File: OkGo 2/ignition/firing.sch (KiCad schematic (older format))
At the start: 43 parts

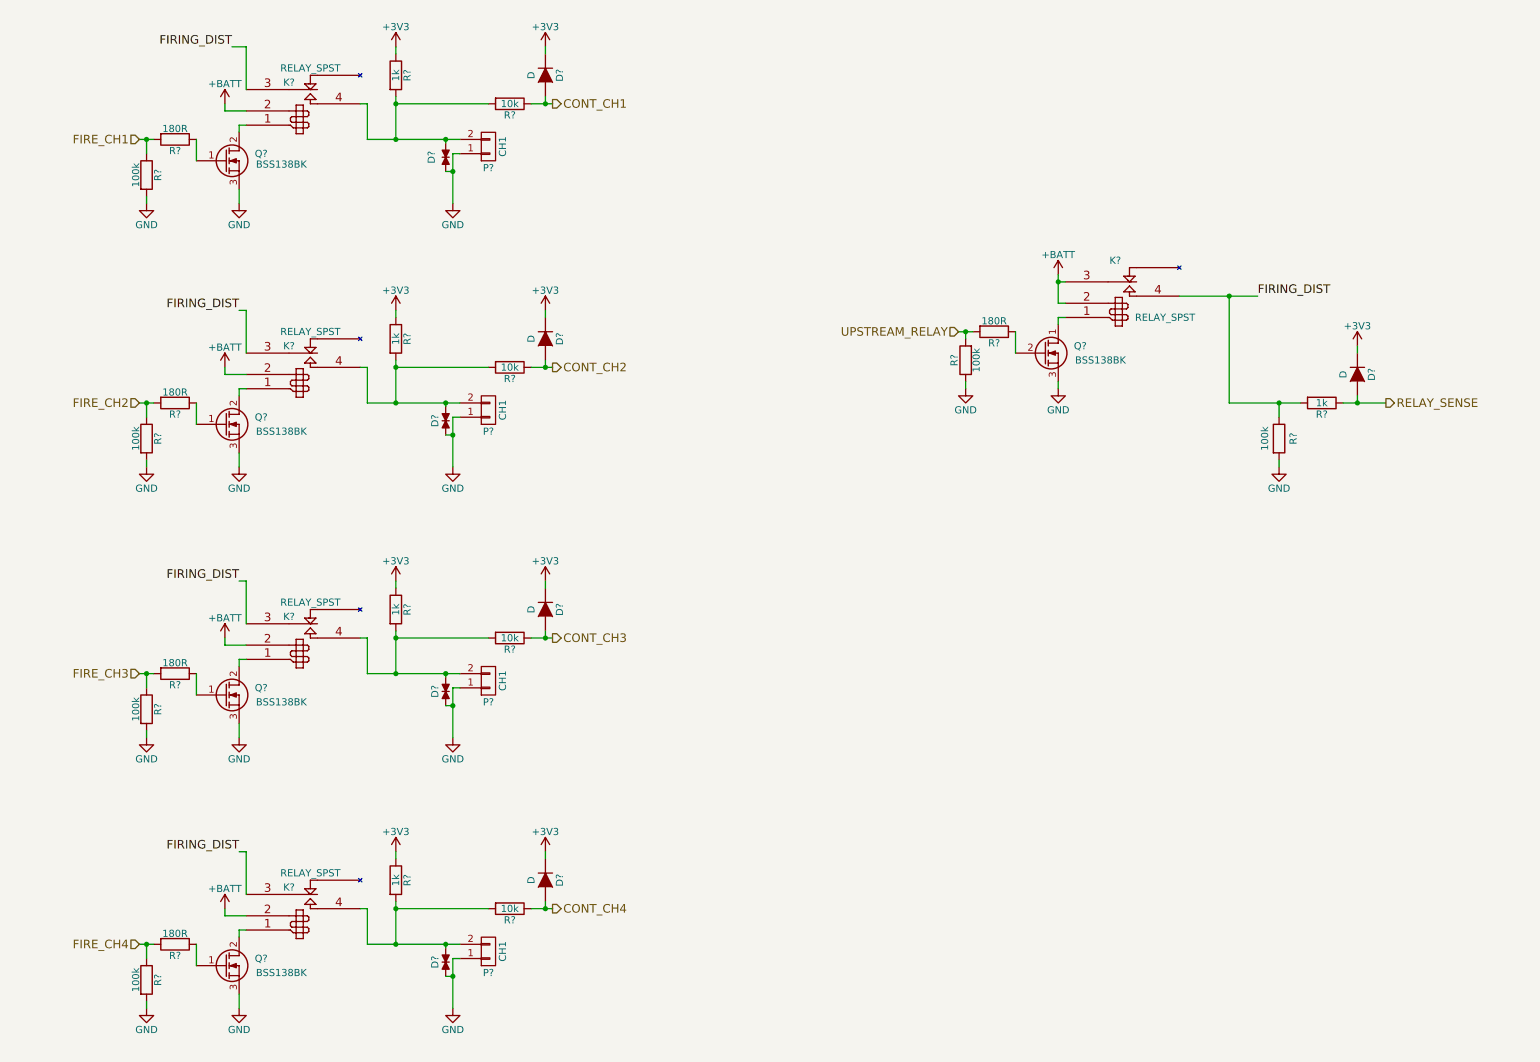
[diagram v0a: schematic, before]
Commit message: Test points. Resolves #14
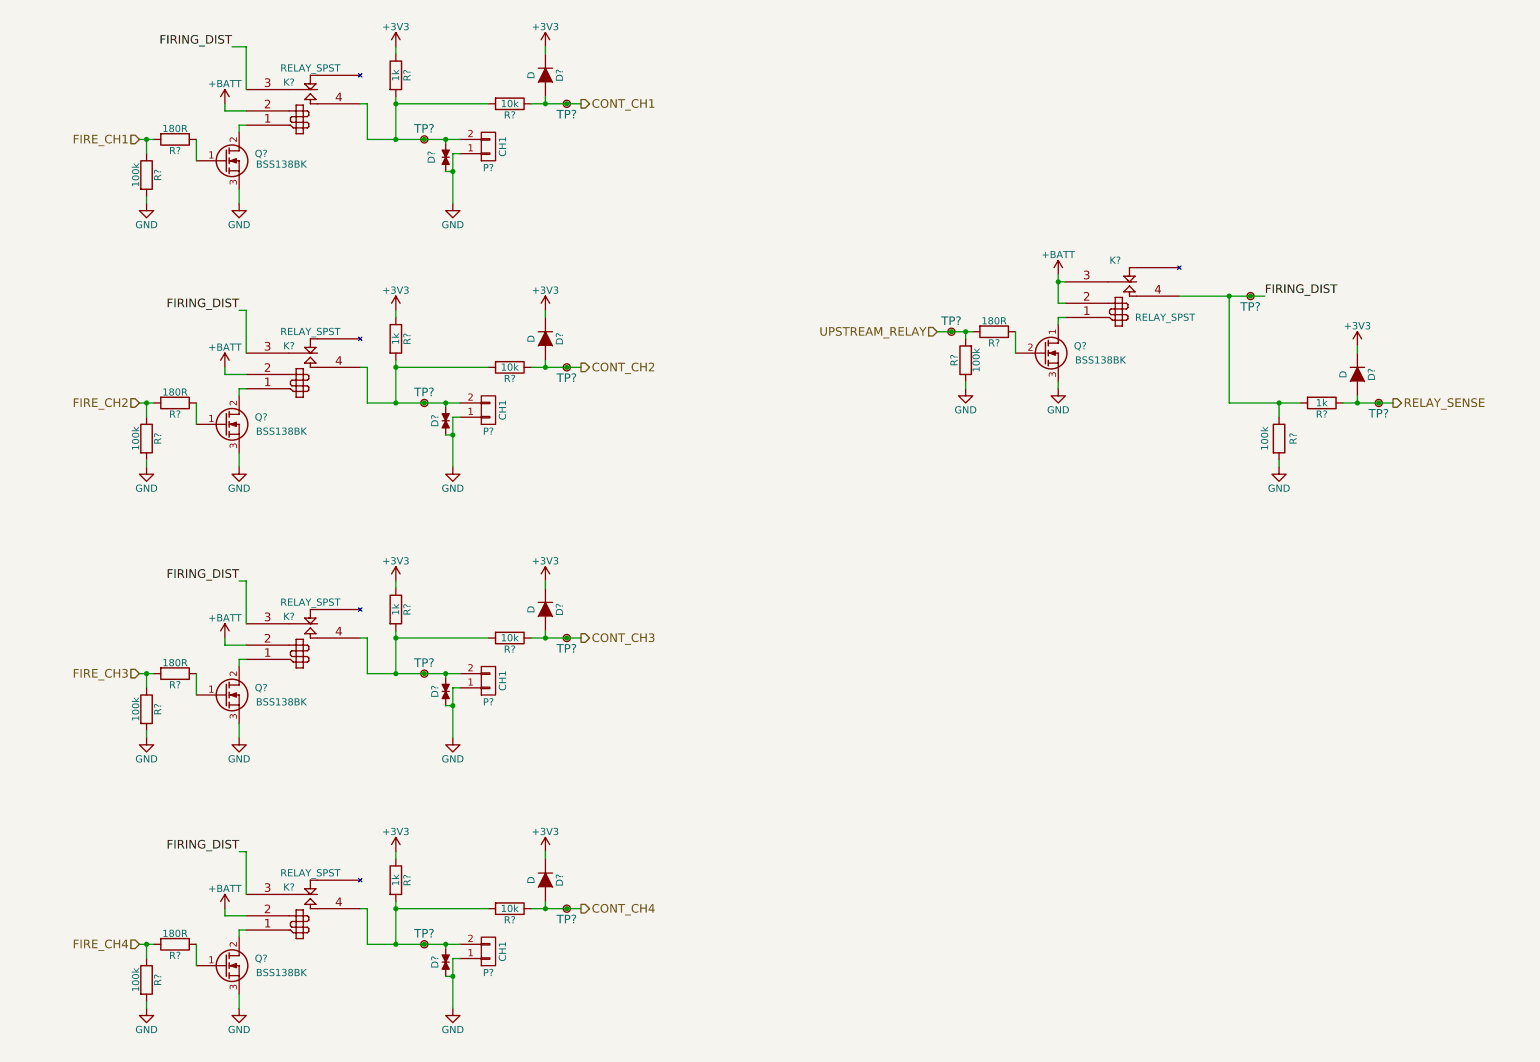
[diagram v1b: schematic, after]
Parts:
- added TP? (x11): TestPoint, symbol TestPoint
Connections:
- net CONT_CH1: now also TP?.1
- net CONT_CH2: now also TP?.1
- net CONT_CH3: now also TP?.1
- net CONT_CH4: now also TP?.1
- net FIRING_DIST: now also TP?.1
- net RELAY_SENSE: now also TP?.1
- net UPSTREAM_RELAY: now also TP?.1
- net at D?.1, K?.4, P?.2 (P2)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: now also TP?.1
- net at D?.2, K?.4, P?.2 (P2)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: now also TP?.1 (x3)
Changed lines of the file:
@@
 LIBS:stm32f071cbt6
 LIBS:tvs_small
+LIBS:testpoint
 LIBS:ignition-cache
 EELAYER 25 0
@@
 	7850 3150 7850 3100
 Wire Wire Line
-	7150 2750 7200 2750
+	7000 2750 7100 2750
+Wire Wire Line
+	7100 2750 7200 2750
 Wire Wire Line
 	7200 2750 7250 2750
@@
 	8700 2500 9050 2500
 Wire Wire Line
-	9050 2500 9250 2500
+	9050 2500 9200 2500
+Wire Wire Line
+	9200 2500 9300 2500
 Wire Wire Line
 	9050 2500 9050 3250
@@
 	9850 3250 9950 3250
 Wire Wire Line
-	9950 3250 10150 3250
+	9950 3250 10100 3250
+Wire Wire Line
+	10100 3250 10200 3250
 $Comp
 L CONN_01X02 P?
@@
 	4150 1150 4250 1150
 Wire Wire Line
-	4250 1150 4300 1150
+	4250 1150 4400 1150
+Wire Wire Line
+	4400 1150 4500 1150
 Wire Wire Line
 	3200 1100 3200 1150
@@
 	4150 3000 4250 3000
 Wire Wire Line
-	4250 3000 4300 3000
+	4250 3000 4400 3000
+Wire Wire Line
+	4400 3000 4500 3000
 Wire Wire Line
 	3200 2950 3200 3000
@@
 	4150 4900 4250 4900
 Wire Wire Line
-	4250 4900 4300 4900
+	4250 4900 4400 4900
+Wire Wire Line
+	4400 4900 4500 4900
 Wire Wire Line
 	3200 4850 3200 4900
@@
 	4150 6800 4250 6800
 Wire Wire Line
-	4250 6800 4300 6800
+	4250 6800 4400 6800
+Wire Wire Line
+	4400 6800 4500 6800
 Wire Wire Line
 	3200 6750 3200 6800
@@
 Wire Wire Line
 	2000 1200 2150 1200
-Text HLabel 4300 1150 2    60   Output ~ 0
+Text HLabel 4500 1150 2    60   Output ~ 0
 CONT_CH1
-Text HLabel 4300 3000 2    60   Output ~ 0
+Text HLabel 4500 3000 2    60   Output ~ 0
 CONT_CH2
-Text HLabel 4300 4900 2    60   Output ~ 0
+Text HLabel 4500 4900 2    60   Output ~ 0
 CONT_CH3
-Text HLabel 4300 6800 2    60   Output ~ 0
+Text HLabel 4500 6800 2    60   Output ~ 0
 CONT_CH4
 Text HLabel 1400 7050 0    60   Input ~ 0
@@
 Text HLabel 1400 1400 0    60   Input ~ 0
 FIRE_CH1
-Text HLabel 7150 2750 0    60   Input ~ 0
+Text HLabel 7000 2750 0    60   Input ~ 0
 UPSTREAM_RELAY
-Text HLabel 10150 3250 2    60   Output ~ 0
+Text HLabel 10200 3250 2    60   Output ~ 0
 RELAY_SENSE
 Text Label 2050 750  2    60   ~ 0
@@
 Text Label 2100 6400 2    60   ~ 0
 FIRING_DIST
-Text Label 9250 2500 0    60   ~ 0
+Text Label 9300 2500 0    60   ~ 0
 FIRING_DIST
+$Comp
+L TestPoint TP?
+U 1 1 559DCEAD
+P 4400 1150
+F 0 "TP?" H 4400 1075 60  0000 C CNN
+F 1 "TestPoint" H 4375 975 60  0001 C CNN
+F 2 "" H 4400 1150 60  0000 C CNN
+F 3 "" H 4400 1150 60  0000 C CNN
+	1    4400 1150
+	1    0    0    -1
+$EndComp
+Connection ~ 4400 1150
+$Comp
+L TestPoint TP?
+U 1 1 559DD237
+P 4400 3000
+F 0 "TP?" H 4400 2925 60  0000 C CNN
+F 1 "TestPoint" H 4375 2825 60  0001 C CNN
+F 2 "" H 4400 3000 60  0000 C CNN
+F 3 "" H 4400 3000 60  0000 C CNN
+	1    4400 3000
+	1    0    0    -1
+$EndComp
+Connection ~ 4400 3000
+$Comp
+L TestPoint TP?
+U 1 1 559DD3E6
+P 4400 4900
+F 0 "TP?" H 4400 4825 60  0000 C CNN
+F 1 "TestPoint" H 4375 4725 60  0001 C CNN
+F 2 "" H 4400 4900 60  0000 C CNN
+F 3 "" H 4400 4900 60  0000 C CNN
+	1    4400 4900
+	1    0    0    -1
+$EndComp
+Connection ~ 4400 4900
+$Comp
+L TestPoint TP?
+U 1 1 559DD5CC
+P 4400 6800
+F 0 "TP?" H 4400 6725 60  0000 C CNN
+F 1 "TestPoint" H 4375 6625 60  0001 C CNN
+F 2 "" H 4400 6800 60  0000 C CNN
+F 3 "" H 4400 6800 60  0000 C CNN
+	1    4400 6800
+	1    0    0    -1
+$EndComp
+Connection ~ 4400 6800
+$Comp
+L TestPoint TP?
+U 1 1 559DDAEE
+P 7100 2750
+F 0 "TP?" H 7100 2675 60  0000 C CNN
+F 1 "TestPoint" H 7075 2575 60  0001 C CNN
+F 2 "" H 7100 2750 60  0000 C CNN
+F 3 "" H 7100 2750 60  0000 C CNN
+	1    7100 2750
+	-1   0    0    1
+$EndComp
+Connection ~ 7100 2750
+$Comp
+L TestPoint TP?
+U 1 1 559DDDE6
+P 10100 3250
+F 0 "TP?" H 10100 3175 60  0000 C CNN
+F 1 "TestPoint" H 10075 3075 60  0001 C CNN
+F 2 "" H 10100 3250 60  0000 C CNN
+F 3 "" H 10100 3250 60  0000 C CNN
+	1    10100 3250
+	1    0    0    -1
+$EndComp
+Connection ~ 10100 3250
+$Comp
+L TestPoint TP?
+U 1 1 559DE049
+P 9200 2500
+F 0 "TP?" H 9200 2425 60  0000 C CNN
+F 1 "TestPoint" H 9175 2325 60  0001 C CNN
+F 2 "" H 9200 2500 60  0000 C CNN
+F 3 "" H 9200 2500 60  0000 C CNN
+	1    9200 2500
+	1    0    0    -1
+$EndComp
+Connection ~ 9200 2500
+$Comp
+L TestPoint TP?
+U 1 1 559DE905
+P 3400 1400
+F 0 "TP?" H 3400 1325 60  0000 C CNN
+F 1 "TestPoint" H 3375 1225 60  0001 C CNN
+F 2 "" H 3400 1400 60  0000 C CNN
+F 3 "" H 3400 1400 60  0000 C CNN
+	1    3400 1400
+	-1   0    0    1
+$EndComp
+Connection ~ 3400 1400
+$Comp
+L TestPoint TP?
+U 1 1 559DF1B5
+P 3400 3250
+F 0 "TP?" H 3400 3175 60  0000 C CNN
+F 1 "TestPoint" H 3375 3075 60  0001 C CNN
+F 2 "" H 3400 3250 60  0000 C CNN
+F 3 "" H 3400 3250 60  0000 C CNN
+	1    3400 3250
+	-1   0    0    1
+$EndComp
+Connection ~ 3400 3250
+$Comp
+L TestPoint TP?
+U 1 1 559DF3AE
+P 3400 5150
+F 0 "TP?" H 3400 5075 60  0000 C CNN
+F 1 "TestPoint" H 3375 4975 60  0001 C CNN
+F 2 "" H 3400 5150 60  0000 C CNN
+F 3 "" H 3400 5150 60  0000 C CNN
+	1    3400 5150
+	-1   0    0    1
+$EndComp
+Connection ~ 3400 5150
+$Comp
+L TestPoint TP?
+U 1 1 559DF5E5
+P 3400 7050
+F 0 "TP?" H 3400 6975 60  0000 C CNN
+F 1 "TestPoint" H 3375 6875 60  0001 C CNN
+F 2 "" H 3400 7050 60  0000 C CNN
+F 3 "" H 3400 7050 60  0000 C CNN
+	1    3400 7050
+	-1   0    0    1
+$EndComp
+Connection ~ 3400 7050
 $EndSCHEMATC

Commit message: Specced/valued/footprinted a lot of parts
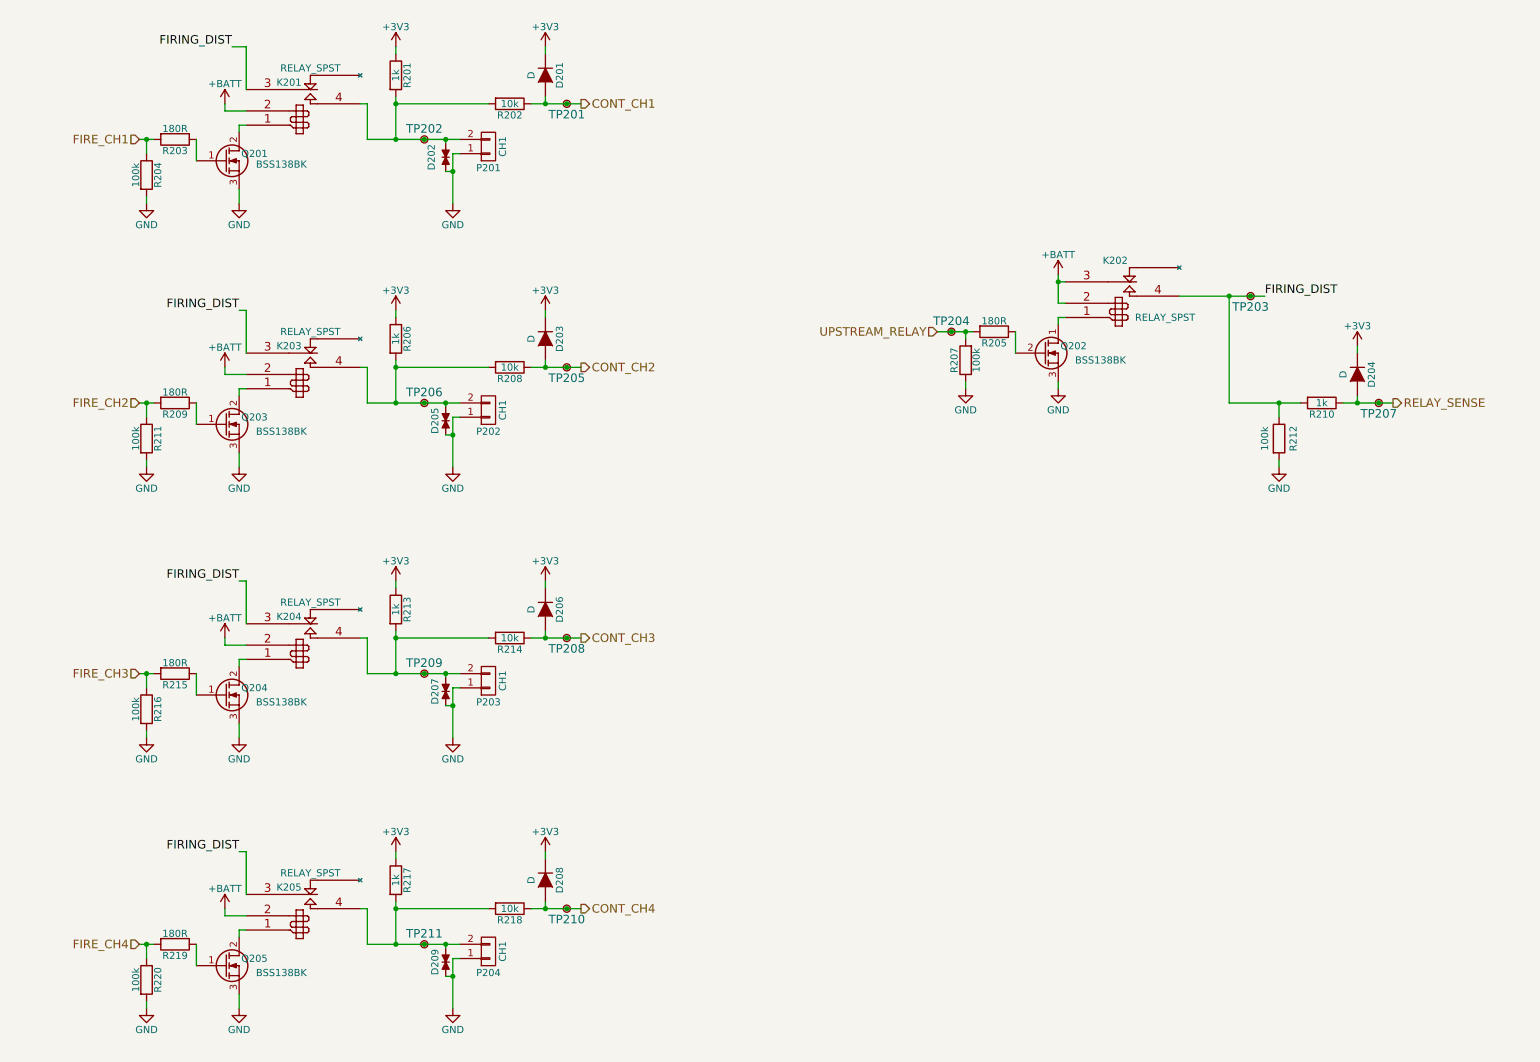
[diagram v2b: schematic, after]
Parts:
- D201, D203, D204, D206, D208: renamed from D?; footprint (none) -> Diodes_SMD:SOD-123; Farnell (none) -> 1510671
- K201, K203, K204, K205: renamed from K?; Farnell 1891999 -> 1629044
- K202: renamed from K?; Farnell (none) -> 1629044
- R201, R206, R210, R213, R217: renamed from R?; footprint (none) -> Resistors_SMD:R_0805_HandSoldering; Farnell (none) -> 2331796
- R202, R208, R214, R218: renamed from R?; footprint (none) -> Resistors_SMD:R_0805_HandSoldering; Farnell (none) -> 2331808
- R203, R205, R209, R215, R219: renamed from R?; footprint (none) -> Resistors_SMD:R_0805_HandSoldering; Farnell (none) -> 2331786
- R204, R207, R211, R212, R216, R220: renamed from R?; footprint (none) -> Resistors_SMD:R_0805_HandSoldering; Farnell (none) -> 2331783
- gave numbers to parts that had none: 24

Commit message: Lots and lots of part selections and small mods
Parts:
- added D?: RED, symbol LED_R
- added D?: GREEN, symbol LED_R
- added D?: BLUE, symbol LED_R
- added D?: WHITE, symbol LED_R
- added P?: CH1, symbol CONN_01X02
- added P?: CH2, symbol CONN_01X02
- added P?: CH3, symbol CONN_01X02
- added P?: CH4, symbol CONN_01X02
- P202: value CH1 -> CH2
- P203: value CH1 -> CH3
- P204: value CH1 -> CH4
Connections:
- new net: D?.1 (K), P?.1 (P1) (x4)
- new net: D?.2 (A), P?.2 (P2) (x4)
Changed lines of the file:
@@
 LIBS:tvs_small
 LIBS:testpoint
+LIBS:sma
+LIBS:led_r
+LIBS:lipo_3s
+LIBS:spst_small
 LIBS:ignition-cache
 EELAYER 25 0
@@
 U 1 1 559E5DC4
 P 3850 1450
-F 0 "P201" H 3850 1600 50  0000 C CNN
-F 1 "CH1" V 3950 1450 50  0000 C CNN
+F 0 "P201" H 3800 1300 50  0000 C CNN
+F 1 "CH1" H 3850 1600 50  0000 C CNN
 F 2 "" H 3850 1450 60  0000 C CNN
 F 3 "" H 3850 1450 60  0000 C CNN
@@
 U 1 1 559E5E1D
 P 3850 3300
-F 0 "P202" H 3850 3450 50  0000 C CNN
-F 1 "CH1" V 3950 3300 50  0000 C CNN
+F 0 "P202" H 3800 3150 50  0000 C CNN
+F 1 "CH2" H 3850 3450 50  0000 C CNN
 F 2 "" H 3850 3300 60  0000 C CNN
 F 3 "" H 3850 3300 60  0000 C CNN
@@
 U 1 1 559E5E76
 P 3850 5200
-F 0 "P203" H 3850 5350 50  0000 C CNN
-F 1 "CH1" V 3950 5200 50  0000 C CNN
+F 0 "P203" H 3800 5050 50  0000 C CNN
+F 1 "CH3" H 3850 5350 50  0000 C CNN
 F 2 "" H 3850 5200 60  0000 C CNN
 F 3 "" H 3850 5200 60  0000 C CNN
@@
 U 1 1 559E5ECF
 P 3850 7100
-F 0 "P204" H 3850 7250 50  0000 C CNN
-F 1 "CH1" V 3950 7100 50  0000 C CNN
+F 0 "P204" H 3800 6950 50  0000 C CNN
+F 1 "CH4" H 3850 7250 50  0000 C CNN
 F 2 "" H 3850 7100 60  0000 C CNN
 F 3 "" H 3850 7100 60  0000 C CNN
@@
 $EndComp
 Connection ~ 3400 7050
+$Comp
+L LED_R D?
+U 1 1 559F6774
+P 4300 1600
+F 0 "D?" H 4275 1725 60  0000 C CNN
+F 1 "RED" H 4250 1800 60  0000 C CNN
+F 2 "" H 4400 1800 60  0000 C CNN
+F 3 "" H 4400 1800 60  0000 C CNN
+F 4 "SC09351" H 4300 1600 60  0001 C CNN "Farnell"
+	1    4300 1600
+	0    1    1    0
+$EndComp
+$Comp
+L CONN_01X02 P?
+U 1 1 559F700F
+P 4000 1450
+F 0 "P?" H 4000 1300 50  0000 C CNN
+F 1 "CH1" H 4000 1600 50  0000 C CNN
+F 2 "" H 4000 1450 60  0000 C CNN
+F 3 "" H 4000 1450 60  0000 C CNN
+	1    4000 1450
+	-1   0    0    1
+$EndComp
+Wire Wire Line
+	4200 1400 4300 1400
+Wire Wire Line
+	4200 1500 4200 1800
+Wire Wire Line
+	4200 1800 4300 1800
+$Comp
+L LED_R D?
+U 1 1 559F7DE2
+P 4300 3450
+F 0 "D?" H 4275 3575 60  0000 C CNN
+F 1 "GREEN" H 4250 3650 60  0000 C CNN
+F 2 "" H 4400 3650 60  0000 C CNN
+F 3 "" H 4400 3650 60  0000 C CNN
+F 4 "SC09352" H 4300 3450 60  0001 C CNN "Farnell"
+	1    4300 3450
+	0    1    1    0
+$EndComp
+$Comp
+L CONN_01X02 P?
+U 1 1 559F7DE8
+P 4000 3300
+F 0 "P?" H 4000 3150 50  0000 C CNN
+F 1 "CH2" H 4000 3450 50  0000 C CNN
+F 2 "" H 4000 3300 60  0000 C CNN
+F 3 "" H 4000 3300 60  0000 C CNN
+	1    4000 3300
+	-1   0    0    1
+$EndComp
+Wire Wire Line
+	4200 3250 4300 3250
+Wire Wire Line
+	4200 3350 4200 3650
+Wire Wire Line
+	4200 3650 4300 3650
+$Comp
+L LED_R D?
+U 1 1 559F8D2C
+P 4300 5350
+F 0 "D?" H 4275 5475 60  0000 C CNN
+F 1 "BLUE" H 4250 5550 60  0000 C CNN
+F 2 "" H 4400 5550 60  0000 C CNN
+F 3 "" H 4400 5550 60  0000 C CNN
+F 4 "SC09354" H 4300 5350 60  0001 C CNN "Farnell"
+	1    4300 5350
+	0    1    1    0
+$EndComp
+$Comp
+L CONN_01X02 P?
+U 1 1 559F8D32
+P 4000 5200
+F 0 "P?" H 4000 5050 50  0000 C CNN
+F 1 "CH3" H 4000 5350 50  0000 C CNN
+F 2 "" H 4000 5200 60  0000 C CNN
+F 3 "" H 4000 5200 60  0000 C CNN
+	1    4000 5200
+	-1   0    0    1
+$EndComp
+Wire Wire Line
+	4200 5150 4300 5150
+Wire Wire Line
+	4200 5250 4200 5550
+Wire Wire Line
+	4200 5550 4300 5550
+$Comp
+L LED_R D?
+U 1 1 559F9C5C
+P 4300 7250
+F 0 "D?" H 4275 7375 60  0000 C CNN
+F 1 "WHITE" H 4250 7450 60  0000 C CNN
+F 2 "" H 4400 7450 60  0000 C CNN
+F 3 "" H 4400 7450 60  0000 C CNN
+F 4 "SC09355" H 4300 7250 60  0001 C CNN "Farnell"
+	1    4300 7250
+	0    1    1    0
+$EndComp
+$Comp
+L CONN_01X02 P?
+U 1 1 559F9C62
+P 4000 7100
+F 0 "P?" H 4000 6950 50  0000 C CNN
+F 1 "CH4" H 4000 7250 50  0000 C CNN
+F 2 "" H 4000 7100 60  0000 C CNN
+F 3 "" H 4000 7100 60  0000 C CNN
+	1    4000 7100
+	-1   0    0    1
+$EndComp
+Wire Wire Line
+	4200 7050 4300 7050
+Wire Wire Line
+	4200 7150 4200 7450
+Wire Wire Line
+	4200 7450 4300 7450
 $EndSCHEMATC
